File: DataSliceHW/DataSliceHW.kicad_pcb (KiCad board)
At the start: 2 copper layers, 85.5 x 54 mm, 97 parts, among them SW1 SKRPABE010, SW10 SKRPABE010, SW11 SKRPABE010, SW12 SKRPABE010, SW13 SKRPABE010, SW14 SKRPABE010, SW15 SKRPABE010, SW16 SKRPABE010, SW17 SKRPABE010, SW18 SKRPABE010, SW19 SKRPABE010, SW2 SKRPABE010, SW20 SKRPABE010, SW21 SKRPABE010, SW22 SKRPABE010, SW23 SKRPABE010, SW24 SKRPABE010, SW25 SKRPABE010, SW26 SKRPABE010, SW27 SKRPABE010, SW28 SKRPABE010, SW29 SKRPABE010, SW3 SKRPABE010, SW30 SKRPABE010, SW31 SKRPABE010, SW32 SKRPABE010, SW33 SKRPABE010, SW34 SKRPABE010, SW35 SKRPABE010, SW36 SKRPABE010, SW37 SKRPABE010, SW38 SKRPABE010, SW39 SKRPABE010, SW4 SKRPABE010, SW40 SKRPABE010, SW41 SKRPABE010, SW42 SKRPABE010, SW43 SKRPABE010, SW44 SKRPABE010, SW45 SKRPABE010, SW46 SKRPABE010, SW47 SKRPABE010, SW48 SKRPABE010, SW5 SKRPABE010, SW6 SKRPABE010, SW7 SKRPABE010, SW8 SKRPABE010, SW9 SKRPABE010, U1 ESP32-C6-WROOM-1-N4

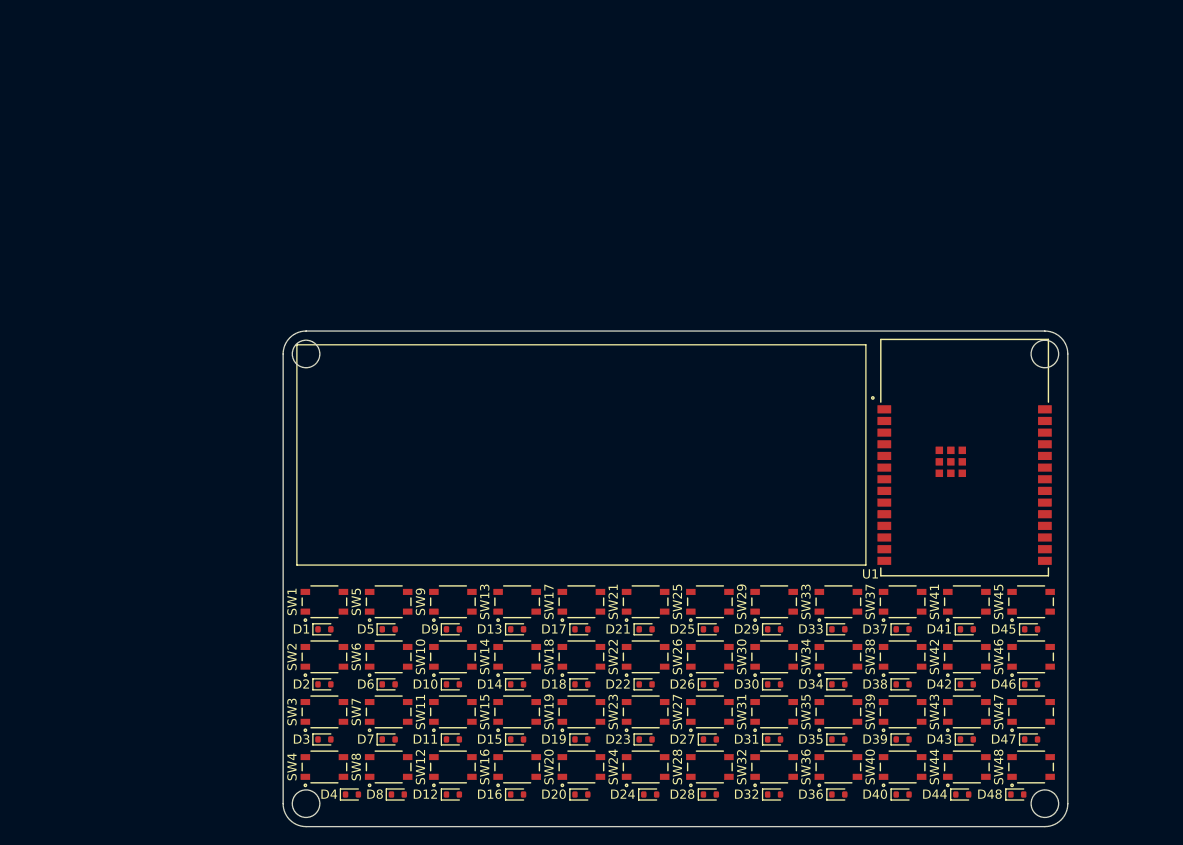
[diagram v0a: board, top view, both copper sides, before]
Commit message: Schematic and PCB progress Changed ESP module to S3 Added Battery outline Added Program buttons, Auto Program schematic, USB-UART without USB-C socket, SD card socket Finished: ESP, Buttons, Programming, SD card TODO: ESP USB UART, OLED, Power/Battery, USB Host, CC1101, LoRa, Ext RS232, Ext SPI
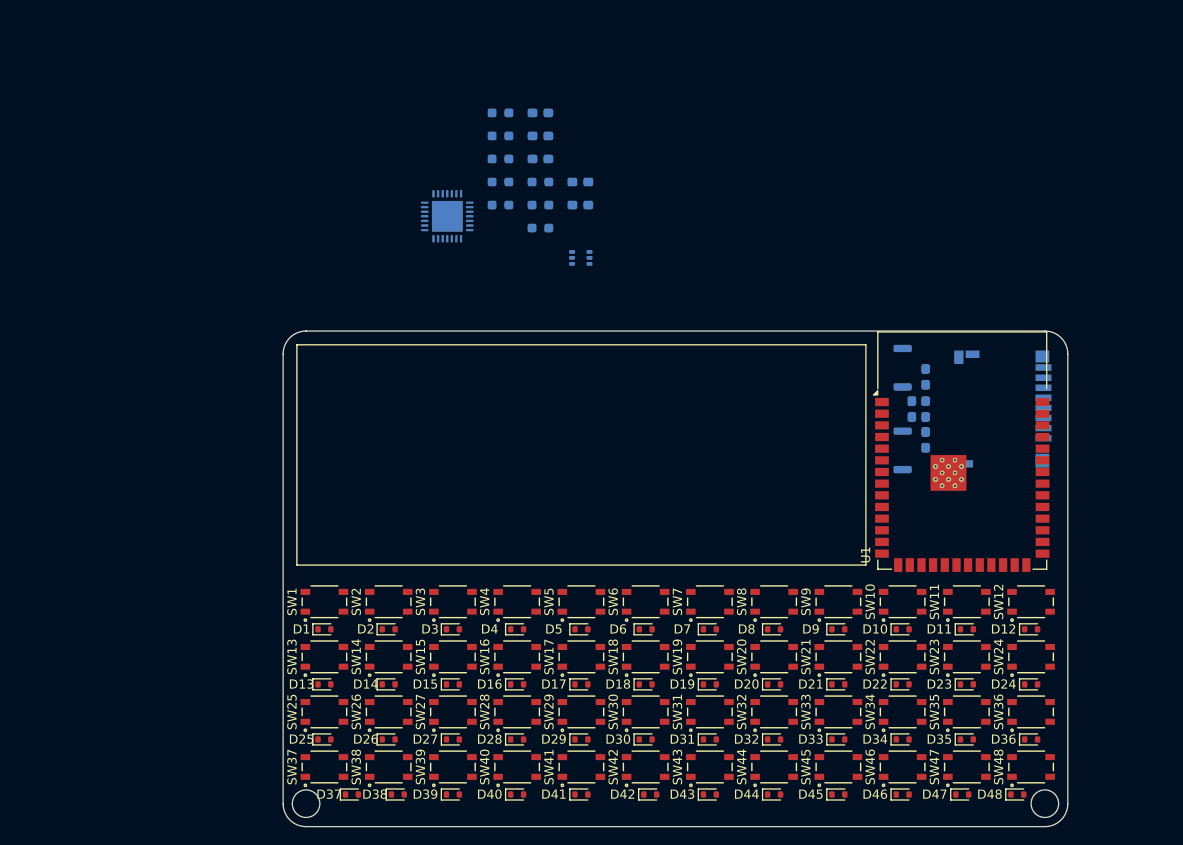
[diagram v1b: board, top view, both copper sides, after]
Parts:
- added C1: 10uF/16V(10%), Capacitor_SMD:C_0603_1608Metric_Pad1.08x0.95mm_HandSolder, B.Cu at (118.5, 58.5)
- added C2: 100nF/16V(10%), Capacitor_SMD:C_0603_1608Metric_Pad1.08x0.95mm_HandSolder, B.Cu at (120.0, 58.5)
- added C3: 100nF/16V(10%), Capacitor_SMD:C_0603_1608Metric_Pad1.08x0.95mm_HandSolder, B.Cu at (120.0, 55.0)
- added C4: 1uF/16V(10%), Capacitor_SMD:C_0603_1608Metric_Pad1.08x0.95mm_HandSolder, B.Cu at (82.4, 33.8)
- added C5: 1uF/16V(10%), Capacitor_SMD:C_0603_1608Metric_Pad1.08x0.95mm_HandSolder, B.Cu at (82.4, 36.3)
- added C6: 1uF/16V(10%), Capacitor_SMD:C_0603_1608Metric_Pad1.08x0.95mm_HandSolder, B.Cu at (120.0, 61.9)
- added C7: 10uF/16V(10%), Capacitor_SMD:C_0603_1608Metric_Pad1.08x0.95mm_HandSolder, B.Cu at (78.0, 26.2)
- added C8: 100nF/16V(10%), Capacitor_SMD:C_0603_1608Metric_Pad1.08x0.95mm_HandSolder, B.Cu at (78.0, 28.7)
- added C9: 4.7uF/16V(10%), Capacitor_SMD:C_0603_1608Metric_Pad1.08x0.95mm_HandSolder, B.Cu at (78.0, 31.2)
- added J1: Micro_SD_Card_Det2, Connector_Card:microSD_HC_Hirose_DM3D-SF, B.Cu at (127.5, 58.5)
- added Q1: BC847BDW1, Package_TO_SOT_SMD:SOT-363_SC-70-6, B.Cu at (82.4, 42.0)
- added R1: 1K(1%), Resistor_SMD:R_0603_1608Metric_Pad0.98x0.95mm_HandSolder, B.Cu at (78.0, 33.8)
- added R2: 24K(1%), Resistor_SMD:R_0603_1608Metric_Pad0.98x0.95mm_HandSolder, B.Cu at (78.0, 36.3)
- added R3: 47K(1%), Resistor_SMD:R_0603_1608Metric_Pad0.98x0.95mm_HandSolder, B.Cu at (78.0, 38.8)
- added R4: 10K(1%), Resistor_SMD:R_0603_1608Metric_Pad0.98x0.95mm_HandSolder, B.Cu at (73.7, 26.2)
- added R5: 10K(1%), Resistor_SMD:R_0603_1608Metric_Pad0.98x0.95mm_HandSolder, B.Cu at (73.7, 28.7)
- added R6: 10K(1%)(NC), Resistor_SMD:R_0603_1608Metric_Pad0.98x0.95mm_HandSolder, B.Cu at (73.7, 31.2)
- added R7: 10K(1%), Resistor_SMD:R_0603_1608Metric_Pad0.98x0.95mm_HandSolder, B.Cu at (73.7, 33.8)
- added R8: 10K(1%), Resistor_SMD:R_0603_1608Metric_Pad0.98x0.95mm_HandSolder, B.Cu at (73.7, 36.3)
- added SW49: SKRKAHE020, Button_Switch_SMD:SW_Push_SPST_NO_Alps_SKRK, B.Cu at (117.5, 54.0)
- added SW50: SKRKAHE020, Button_Switch_SMD:SW_Push_SPST_NO_Alps_SKRK, B.Cu at (117.5, 63.0)
- added U2: CP2102N-Axx-xQFN28, Package_DFN_QFN:QFN-28-1EP_5x5mm_P0.5mm_EP3.35x3.35mm, B.Cu at (67.9, 37.5)
- U1: value ESP32-C6-WROOM-1-N4 -> ESP32-S3-WROOM-1; footprint DataSlice:MOD28_ESP32-C6-WROOM-1_EXP -> RF_Module:ESP32-S3-WROOM-1
- moved U1 0.83 mm to (124.0, 63.0)
- renumbered D37 to D10, D41 to D11, D45 to D12, D2 to D13, D6 to D14, D10 to D15, D14 to D16, D18 to D17, D22 to D18, D26 to D19, D5 to D2, D30 to D20, D34 to D21, D38 to D22, D42 to D23, D46 to D24, D3 to D25, D7 to D26, D11 to D27, D15 to D28, D19 to D29, D9 to D3, D23 to D30, D27 to D31, D31 to D32, D35 to D33, D39 to D34, D43 to D35, D47 to D36, D4 to D37, D8 to D38, D12 to D39, D13 to D4, D16 to D40, D20 to D41, D24 to D42, D28 to D43, D32 to D44, D36 to D45, D40 to D46, D44 to D47, D17 to D5, D21 to D6, D25 to D7, D29 to D8, D33 to D9, SW37 to SW10, SW41 to SW11, SW45 to SW12, SW2 to SW13, SW6 to SW14, SW10 to SW15, SW14 to SW16, SW18 to SW17, SW22 to SW18, SW26 to SW19, SW5 to SW2, SW30 to SW20, SW34 to SW21, SW38 to SW22, SW42 to SW23, SW46 to SW24, SW3 to SW25, SW7 to SW26, SW11 to SW27, SW15 to SW28, SW19 to SW29, SW9 to SW3, SW23 to SW30, SW27 to SW31, SW31 to SW32, SW35 to SW33, SW39 to SW34, SW43 to SW35, SW47 to SW36, SW4 to SW37, SW8 to SW38, SW12 to SW39, SW13 to SW4, SW16 to SW40, SW20 to SW41, SW24 to SW42, SW28 to SW43, SW32 to SW44, SW36 to SW45, SW40 to SW46, SW44 to SW47, SW17 to SW5, SW21 to SW6, SW25 to SW7, SW29 to SW8, SW33 to SW9
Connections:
- D1 pad 1: Row1 -> /KB_R_0
- D10 pad 1: Row1 -> /KB_R_0
- D11 pad 1: Row1 -> /KB_R_0
- D12 pad 1: Row1 -> /KB_R_0
- D13 pad 1: Row2 -> /KB_R_1
- D14 pad 1: Row2 -> /KB_R_1
- D15 pad 1: Row2 -> /KB_R_1
- D16 pad 1: Row2 -> /KB_R_1
- D17 pad 1: Row2 -> /KB_R_1
- D18 pad 1: Row2 -> /KB_R_1
- D19 pad 1: Row2 -> /KB_R_1
- D2 pad 1: Row1 -> /KB_R_0
- D20 pad 1: Row2 -> /KB_R_1
- D21 pad 1: Row2 -> /KB_R_1
- D22 pad 1: Row2 -> /KB_R_1
- D23 pad 1: Row2 -> /KB_R_1
- D24 pad 1: Row2 -> /KB_R_1
- D25 pad 1: Row3 -> /KB_R_2
- D26 pad 1: Row3 -> /KB_R_2
- D27 pad 1: Row3 -> /KB_R_2
- D28 pad 1: Row3 -> /KB_R_2
- D29 pad 1: Row3 -> /KB_R_2
- D3 pad 1: Row1 -> /KB_R_0
- D30 pad 1: Row3 -> /KB_R_2
- D31 pad 1: Row3 -> /KB_R_2
- D32 pad 1: Row3 -> /KB_R_2
- D33 pad 1: Row3 -> /KB_R_2
- D34 pad 1: Row3 -> /KB_R_2
- D35 pad 1: Row3 -> /KB_R_2
- D36 pad 1: Row3 -> /KB_R_2
- D37 pad 1: Row4 -> /KB_R_3
- D38 pad 1: Row4 -> /KB_R_3
- D39 pad 1: Row4 -> /KB_R_3
- D4 pad 1: Row1 -> /KB_R_0
- D40 pad 1: Row4 -> /KB_R_3
- D41 pad 1: Row4 -> /KB_R_3
- D42 pad 1: Row4 -> /KB_R_3
- D43 pad 1: Row4 -> /KB_R_3
- D44 pad 1: Row4 -> /KB_R_3
- D45 pad 1: Row4 -> /KB_R_3
- D46 pad 1: Row4 -> /KB_R_3
- D47 pad 1: Row4 -> /KB_R_3
- D48 pad 1: Row4 -> /KB_R_3
- D5 pad 1: Row1 -> /KB_R_0
- D6 pad 1: Row1 -> /KB_R_0
- D7 pad 1: Row1 -> /KB_R_0
- D8 pad 1: Row1 -> /KB_R_0
- D9 pad 1: Row1 -> /KB_R_0
- SW1 pad 1: Col1 -> /KB_C_0
- SW1 pad 2: Col1 -> /KB_C_0
- SW10 pad 1: Col10 -> /KB_C_9
- SW10 pad 2: Col10 -> /KB_C_9
- SW11 pad 1: Col11 -> /KB_C_10
- SW11 pad 2: Col11 -> /KB_C_10
- SW12 pad 1: Col12 -> /KB_C_11
- SW12 pad 2: Col12 -> /KB_C_11
- SW13 pad 1: Col1 -> /KB_C_0
- SW13 pad 2: Col1 -> /KB_C_0
- SW14 pad 1: Col2 -> /KB_C_1
- SW14 pad 2: Col2 -> /KB_C_1
- SW15 pad 1: Col3 -> /KB_C_2
- SW15 pad 2: Col3 -> /KB_C_2
- SW16 pad 1: Col4 -> /KB_C_3
- SW16 pad 2: Col4 -> /KB_C_3
- SW17 pad 1: Col5 -> /KB_C_4
- SW17 pad 2: Col5 -> /KB_C_4
- SW18 pad 1: Col6 -> /KB_C_5
- SW18 pad 2: Col6 -> /KB_C_5
- SW19 pad 1: Col7 -> /KB_C_6
- SW19 pad 2: Col7 -> /KB_C_6
- SW2 pad 1: Col2 -> /KB_C_1
- SW2 pad 2: Col2 -> /KB_C_1
- SW20 pad 1: Col8 -> /KB_C_7
- SW20 pad 2: Col8 -> /KB_C_7
- SW21 pad 1: Col9 -> /KB_C_8
- SW21 pad 2: Col9 -> /KB_C_8
- SW22 pad 1: Col10 -> /KB_C_9
- SW22 pad 2: Col10 -> /KB_C_9
- SW23 pad 1: Col11 -> /KB_C_10
- SW23 pad 2: Col11 -> /KB_C_10
- SW24 pad 1: Col12 -> /KB_C_11
- SW24 pad 2: Col12 -> /KB_C_11
- SW25 pad 1: Col1 -> /KB_C_0
- SW25 pad 2: Col1 -> /KB_C_0
- SW26 pad 1: Col2 -> /KB_C_1
- SW26 pad 2: Col2 -> /KB_C_1
- SW27 pad 1: Col3 -> /KB_C_2
- SW27 pad 2: Col3 -> /KB_C_2
- SW28 pad 1: Col4 -> /KB_C_3
- SW28 pad 2: Col4 -> /KB_C_3
- SW29 pad 1: Col5 -> /KB_C_4
- SW29 pad 2: Col5 -> /KB_C_4
- SW3 pad 1: Col3 -> /KB_C_2
- SW3 pad 2: Col3 -> /KB_C_2
- SW30 pad 1: Col6 -> /KB_C_5
- SW30 pad 2: Col6 -> /KB_C_5
- SW31 pad 1: Col7 -> /KB_C_6
- SW31 pad 2: Col7 -> /KB_C_6
- SW32 pad 1: Col8 -> /KB_C_7
- SW32 pad 2: Col8 -> /KB_C_7
- SW33 pad 1: Col9 -> /KB_C_8
- SW33 pad 2: Col9 -> /KB_C_8
- SW34 pad 1: Col10 -> /KB_C_9
- SW34 pad 2: Col10 -> /KB_C_9
- SW35 pad 1: Col11 -> /KB_C_10
- SW35 pad 2: Col11 -> /KB_C_10
- SW36 pad 1: Col12 -> /KB_C_11
- SW36 pad 2: Col12 -> /KB_C_11
- SW37 pad 1: Col1 -> /KB_C_0
- SW37 pad 2: Col1 -> /KB_C_0
- SW38 pad 1: Col2 -> /KB_C_1
- SW38 pad 2: Col2 -> /KB_C_1
- SW39 pad 1: Col3 -> /KB_C_2
- SW39 pad 2: Col3 -> /KB_C_2
- SW4 pad 1: Col4 -> /KB_C_3
- SW4 pad 2: Col4 -> /KB_C_3
- SW40 pad 1: Col4 -> /KB_C_3
- SW40 pad 2: Col4 -> /KB_C_3
- SW41 pad 1: Col5 -> /KB_C_4
- SW41 pad 2: Col5 -> /KB_C_4
- SW42 pad 1: Col6 -> /KB_C_5
- SW42 pad 2: Col6 -> /KB_C_5
- SW43 pad 1: Col7 -> /KB_C_6
- SW43 pad 2: Col7 -> /KB_C_6
- SW44 pad 1: Col8 -> /KB_C_7
- SW44 pad 2: Col8 -> /KB_C_7
- SW45 pad 1: Col9 -> /KB_C_8
- SW45 pad 2: Col9 -> /KB_C_8
- SW46 pad 1: Col10 -> /KB_C_9
- SW46 pad 2: Col10 -> /KB_C_9
- SW47 pad 1: Col11 -> /KB_C_10
- SW47 pad 2: Col11 -> /KB_C_10
- SW48 pad 1: Col12 -> /KB_C_11
- SW48 pad 2: Col12 -> /KB_C_11
- SW5 pad 1: Col5 -> /KB_C_4
- SW5 pad 2: Col5 -> /KB_C_4
- SW6 pad 1: Col6 -> /KB_C_5
- SW6 pad 2: Col6 -> /KB_C_5
- SW7 pad 1: Col7 -> /KB_C_6
- SW7 pad 2: Col7 -> /KB_C_6
- SW8 pad 1: Col8 -> /KB_C_7
- SW8 pad 2: Col8 -> /KB_C_7
- SW9 pad 1: Col9 -> /KB_C_8
- SW9 pad 2: Col9 -> /KB_C_8
- U1 pad 1: unconnected-(U1-GND-Pad1) -> GND
- U1 pad 10: unconnected-(U1-IO8-Pad10) -> /RS_TX
- U1 pad 11: unconnected-(U1-IO10-Pad11) -> /RS_RX
- U1 pad 12: unconnected-(U1-IO11-Pad12) -> /KB_C_7
- U1 pad 13: unconnected-(U1-IO12-Pad13) -> /HOST_DN
- U1 pad 14: unconnected-(U1-IO13-Pad14) -> /HOST_DP
- U1 pad 15: unconnected-(U1-IO9-Pad15) -> /KB_C_2
- U1 pad 16: unconnected-(U1-IO18-Pad16) -> /KB_R_1
- U1 pad 17: unconnected-(U1-IO19-Pad17) -> /KB_C_8
- U1 pad 18: unconnected-(U1-IO20-Pad18) -> /SPI_CS
- U1 pad 19: unconnected-(U1-IO21-Pad19) -> /SPI_DI
- U1 pad 2: unconnected-(U1-3V3-Pad2) -> VCC
- U1 pad 20: unconnected-(U1-IO22-Pad20) -> /SPI_CK
- U1 pad 21: unconnected-(U1-IO23-Pad21) -> /SPI_DO
- U1 pad 22: unconnected-(U1-NC-Pad22) -> /KB_C_9
- U1 pad 23: unconnected-(U1-IO15-Pad23) -> /SD_CLK
- U1 pad 24: unconnected-(U1-RXD0-Pad24) -> /KB_R_2
- U1 pad 25: unconnected-(U1-TXD0-Pad25) -> /KB_R_3
- U1 pad 26: unconnected-(U1-IO3-Pad26) -> /KB_R_0
- U1 pad 27: unconnected-(U1-IO2-Pad27) -> /GPIO0
- U1 pad 3: unconnected-(U1-EN-Pad3) -> /ESP_EN
- U1 pad 31: unconnected-(U1-GND-Pad31) -> /SD_CMD
- U1 pad 32: unconnected-(U1-GND-Pad32) -> /SD_D0
- U1 pad 33: unconnected-(U1-GND-Pad33) -> /SD_D1
- U1 pad 34: unconnected-(U1-GND-Pad34) -> /SD_D2
- U1 pad 35: unconnected-(U1-GND-Pad35) -> /SD_D3
- U1 pad 36: unconnected-(U1-GND-Pad36) -> /UART_RX
- U1 pad 37: unconnected-(U1-GND-Pad37) -> /UART_TX
- U1 pad 4: unconnected-(U1-IO4-Pad4) -> /KB_C_3
- U1 pad 5: unconnected-(U1-IO5-Pad5) -> /KB_C_4
- U1 pad 6: unconnected-(U1-IO6-Pad6) -> /KB_C_5
- U1 pad 7: unconnected-(U1-IO7-Pad7) -> /KB_C_6
- U1 pad 8: unconnected-(U1-IO0-Pad8) -> /KB_C_10
- U1 pad 9: unconnected-(U1-IO1-Pad9) -> /KB_C_11
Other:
- outline, holes or cut-outs redrawn

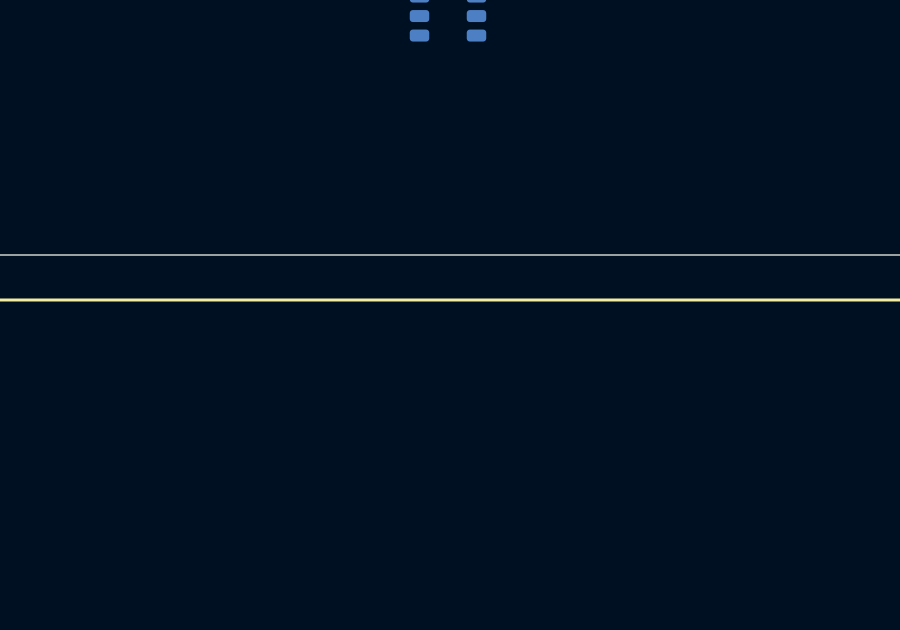
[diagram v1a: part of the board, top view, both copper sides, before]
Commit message: Pin adjustments for SD Add display ribbon cable hole
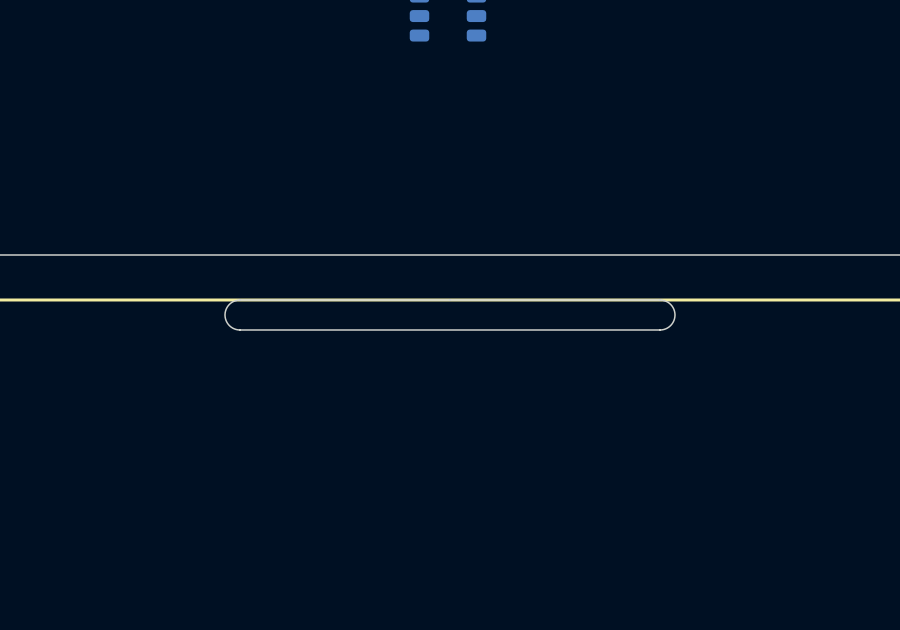
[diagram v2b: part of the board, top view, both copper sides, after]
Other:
- outline, holes or cut-outs redrawn
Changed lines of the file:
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@@
+		(layer "Edge.Cuts")
+	)
+	(gr_arc
+		(start 89.5 51.5)
+		(mid 90 52)
+		(end 89.5 52.5)
+		(stroke
+			(width 0.05)
+			(type default)
+		)
 		(layer "Edge.Cuts")
 	)
@@
 		)
 		(fill no)
+		(layer "Edge.Cuts")
+	)
+	(gr_line
+		(start 82.5 51.5)
+		(end 89.5 51.5)
+		(stroke
+			(width 0.05)
+			(type default)
+		)
 		(layer "Edge.Cuts")
 	)
@@
 		(layer "Edge.Cuts")
 	)
+	(gr_line
+		(start 82.5 51.5)
+		(end 75.5 51.5)
+		(stroke
+			(width 0.05)
+			(type default)
+		)
+		(layer "Edge.Cuts")
+	)
 	(gr_arc
 		(start 52.5 104)
@@
 		(start 50 101.5)
 		(end 50 52.5)
+		(stroke
+			(width 0.05)
+			(type default)
+		)
+		(layer "Edge.Cuts")
+	)
+	(gr_line
+		(start 75.5 52.5)
+		(end 89.5 52.5)
 		(stroke
 			(width 0.05)
@@
 		(stroke
 			(width 0.05)
+			(type default)
+		)
+		(layer "Edge.Cuts")
+	)
+	(gr_arc
+		(start 75.5 52.5)
+		(mid 75 52)
+		(end 75.5 51.5)
+		(stroke
+			(width 0.05)
